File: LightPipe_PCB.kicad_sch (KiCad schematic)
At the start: 10 parts, among them X1 KLB-4, X2 KLB-4, X3 XT30, X4.1 Cable-0.7mm, X4.2 Cable-0.7mm, X5.1 Cable-1.5mm, X5.2 Cable-1.5mm

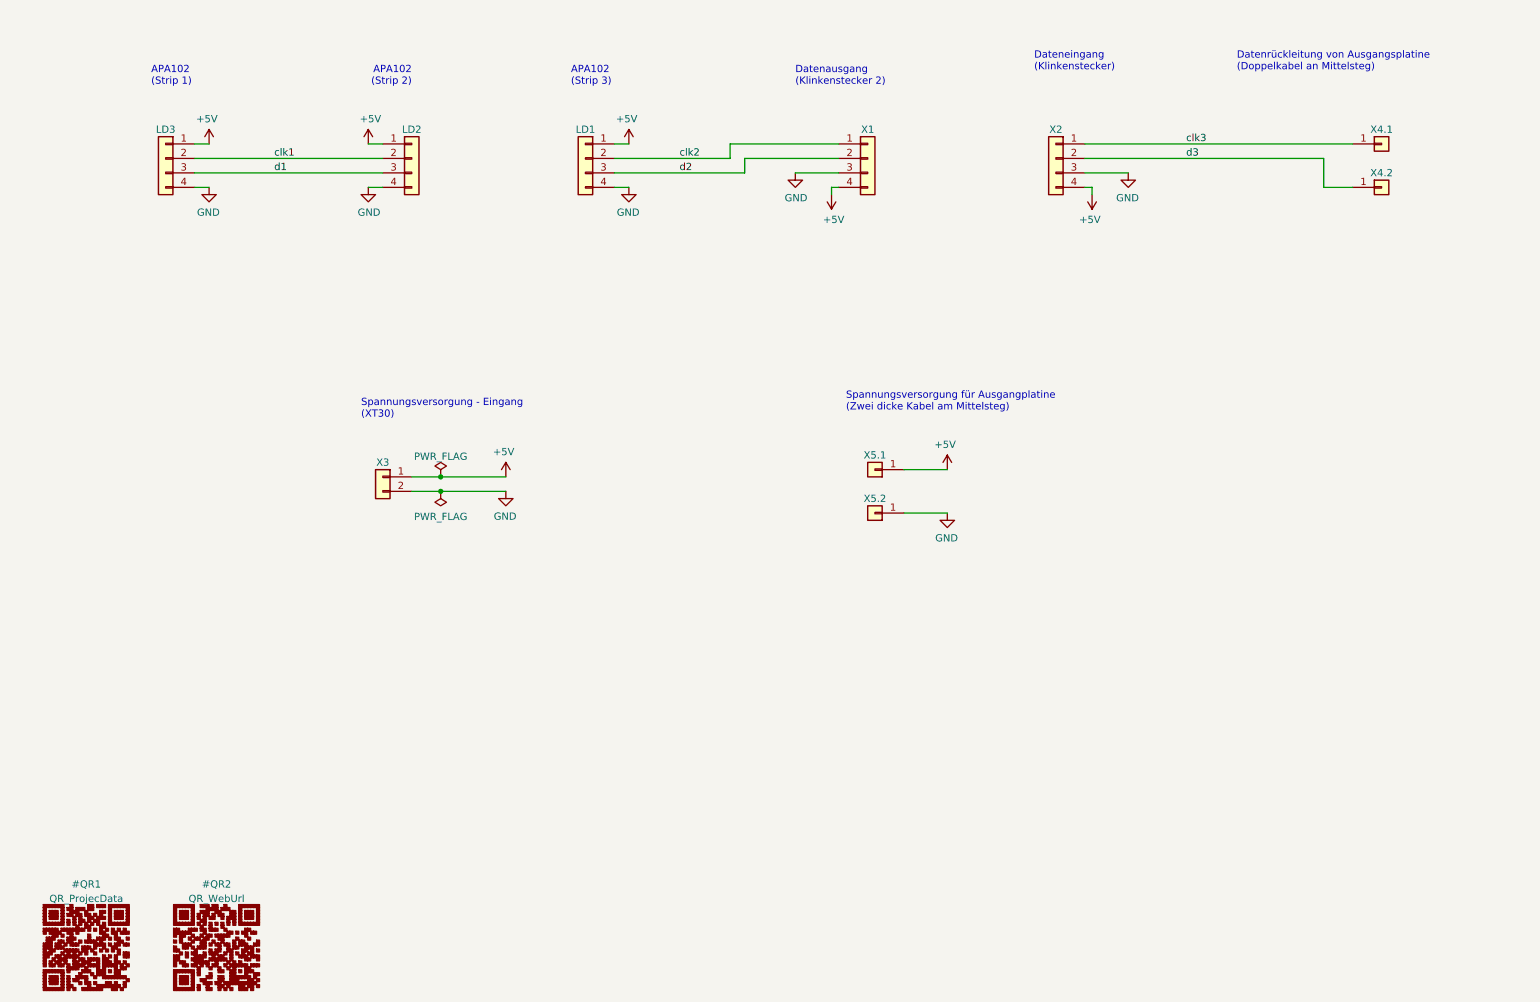
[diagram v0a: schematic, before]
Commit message: [clean] Optimized schematic to be easy readable as input PCB | changed 3D bodys in PCB to Input PCB positions | update date, company, project name and QR-code in schematic and board
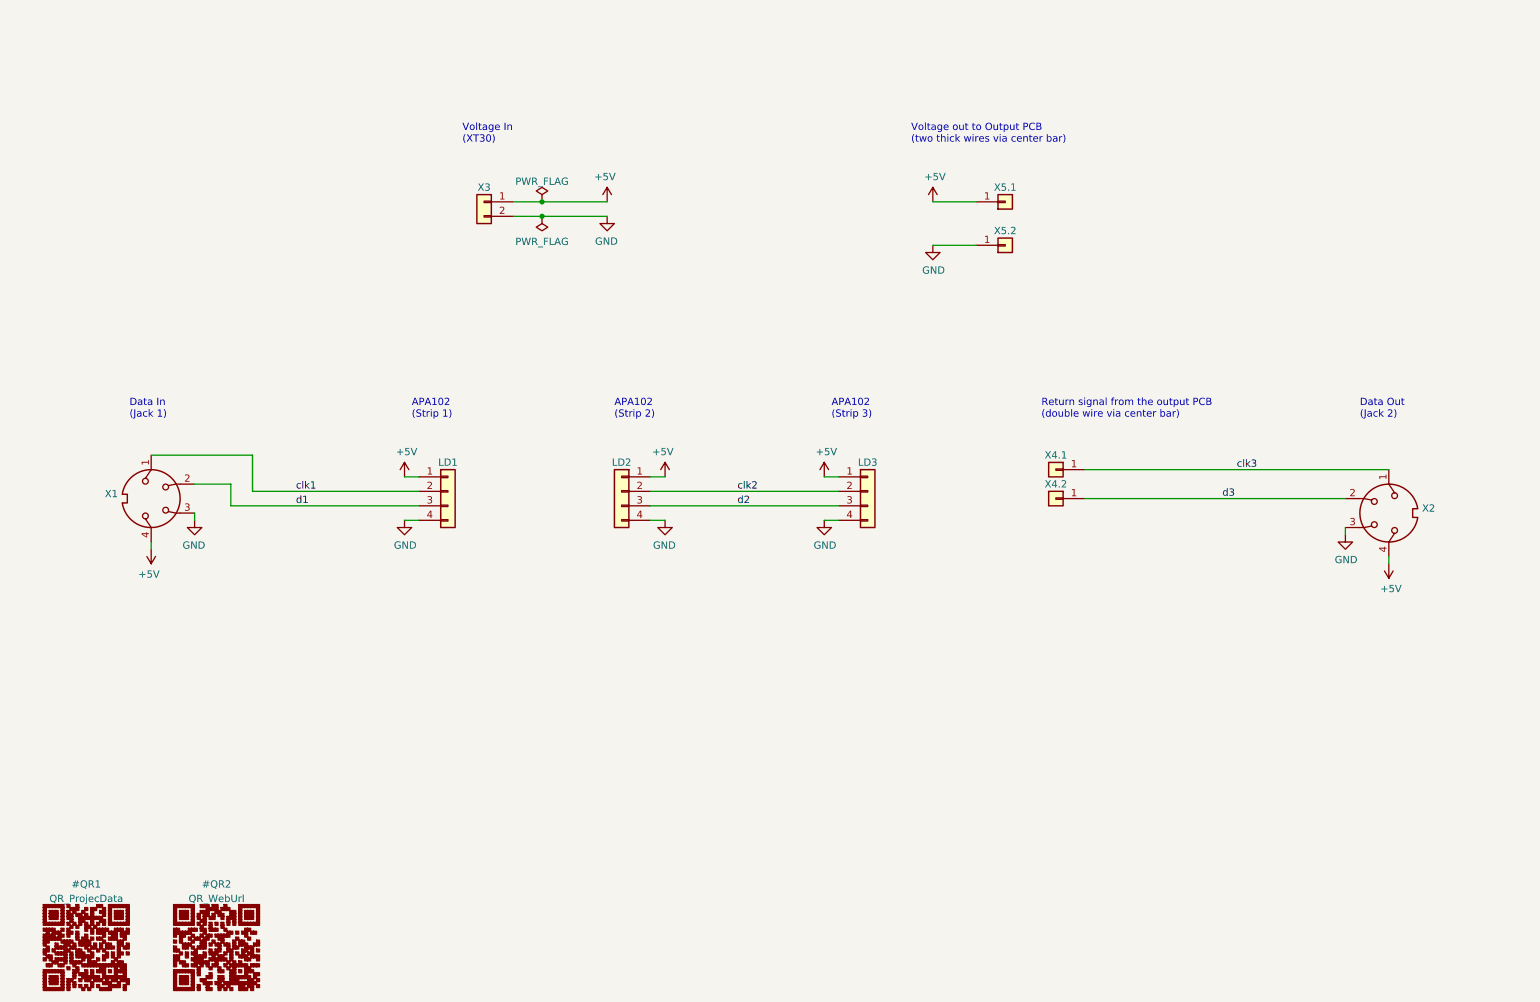
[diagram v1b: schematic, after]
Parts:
- removed X1, X2: KLB-4, h8-Connectors:Lumberg-KLB-4-Klinkensteckverbinder-3_5-180deg-turnable, symbol Connector_Generic:Conn_01x04
- added X1, X2: KLB-4, h8-Connectors:Lumberg-KLB-4-Klinkensteckverbinder-3_5-180deg-turnable, symbol Connector:DIN-4
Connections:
- net +5V: now also X1.4, X2.4
- net GND: now also X1.3, X2.3
- net clk1: now also LD1.2 (Pin_2), X1.1; no longer LD2.2 (Pin_2), LD3.2 (Pin_2)
- net clk2: now also LD2.2 (Pin_2), LD3.2 (Pin_2); no longer LD1.2 (Pin_2)
- net clk3: now also X2.1
- net d1: now also LD1.3 (Pin_3), X1.2; no longer LD2.3 (Pin_3), LD3.3 (Pin_3)
- net d2: now also LD2.3 (Pin_3), LD3.3 (Pin_3); no longer LD1.3 (Pin_3)
- net d3: now also X2.2
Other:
- note added: "Data In (Jack 1)"
- note added: "Data Out (Jack 2)"
- note added: "Return signal from the output PCB (double wire via center bar)"
- note added: "Voltage In (XT30)"
- note added: "Voltage out to Output PCB (two thick wires via center bar)"
- note removed: "Datenausgang (Klinkenstecker 2)"
- note removed: "Dateneingang (Klinkenstecker)"
- note removed: "Datenrückleitung von Ausgangsplatine (Doppelkabel an Mittelsteg)"
- note removed: "Spannungsversorgung - Eingang (XT30)"
- note removed: "Spannungsversorgung für Ausgangplatine (Zwei dicke Kabel am Mittelsteg)"
- company: CCC Göttingen -> HansAchterbahn
- title: LightPipe - StripeConnector -> LightPipe Input/Output PCB
- moved on the sheet: LD1, LD2, LD3, X3, X4.1, X4.2, X5.1, X5.2

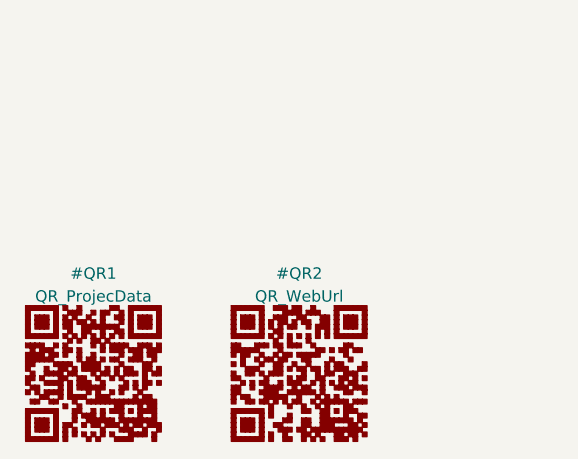
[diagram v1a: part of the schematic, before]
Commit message: [DRC] Solved DRC errors
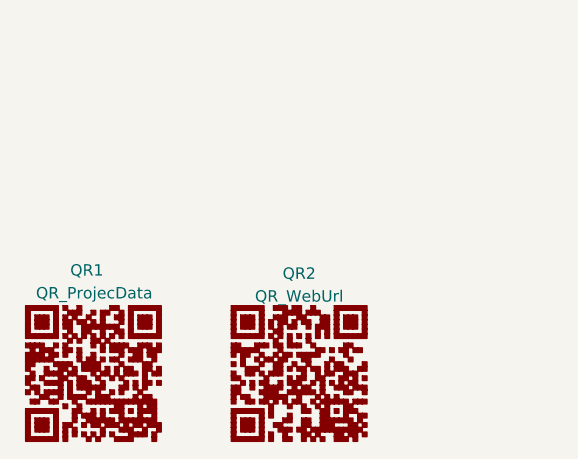
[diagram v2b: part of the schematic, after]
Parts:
- added QR1: QR_ProjecData, QR:QR_ProjecData, symbol QR_Lib:QR_ProjecData
- added QR2: QR_WebUrl, QR:QR_WebUrl, symbol QR_Lib:QR_WebUrl
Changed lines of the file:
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@@
   )
   (symbol (lib_id "QR_Lib:QR_ProjecData") (at 27.94 184.15 0) (unit 1)
-    (in_bom no) (on_board yes) (fields_autoplaced)
-    (property "Reference" "#QR1" (id 0) (at 27.98 173.0767 0))
-    (property "Value" "QR_ProjecData" (id 1) (at 27.98 175.6136 0))
+    (in_bom no) (on_board yes)
+    (property "Reference" "QR1" (id 0) (at 25.4 172.72 0)
+      (effects (font (size 1.27 1.27)) (justify left))
+    )
+    (property "Value" "QR_ProjecData" (id 1) (at 21.59 175.26 0)
+      (effects (font (size 1.27 1.27)) (justify left))
+    )
     (property "Footprint" "QR:QR_ProjecData" (id 2) (at 27.94 194.6 0)
       (effects (font (size 1.27 1.27)) hide)
@@
   (symbol (lib_id "QR_Lib:QR_WebUrl") (at 50.8 184.15 0) (unit 1)
     (in_bom no) (on_board yes) (fields_autoplaced)
-    (property "Reference" "#QR2" (id 0) (at 50.84 173.0767 0))
+    (property "Reference" "QR2" (id 0) (at 50.84 173.0767 0))
     (property "Value" "QR_WebUrl" (id 1) (at 50.84 175.6136 0))
     (property "Footprint" "QR:QR_WebUrl" (id 2) (at 50.8 194.6 0)
@@
       (reference "#PWR?") (unit 1) (value "+5V") (footprint "")
     )
-    (path "/8ca2c3de-1205-4532-8a76-d9c1a6b1f484"
-      (reference "#QR1") (unit 1) (value "QR_ProjecData") (footprint "QR:QR_ProjecData")
-    )
-    (path "/cb914536-84d3-4fd6-ba86-3661b57a5b27"
-      (reference "#QR2") (unit 1) (value "QR_WebUrl") (footprint "QR:QR_WebUrl")
-    )
     (path "/00000000-0000-0000-0000-00005f94ae24"
       (reference "LD1") (unit 1) (value "APA102") (footprint "h8-Connectors:APA102-Strip-Output")
@@
       (reference "LD3") (unit 1) (value "APA102") (footprint "h8-Connectors:APA102-Strip-Output")
     )
+    (path "/8ca2c3de-1205-4532-8a76-d9c1a6b1f484"
+      (reference "QR1") (unit 1) (value "QR_ProjecData") (footprint "QR:QR_ProjecData")
+    )
+    (path "/cb914536-84d3-4fd6-ba86-3661b57a5b27"
+      (reference "QR2") (unit 1) (value "QR_WebUrl") (footprint "QR:QR_WebUrl")
+    )
     (path "/c2774b4d-69cb-4b83-93d8-9a28fe6279cf"

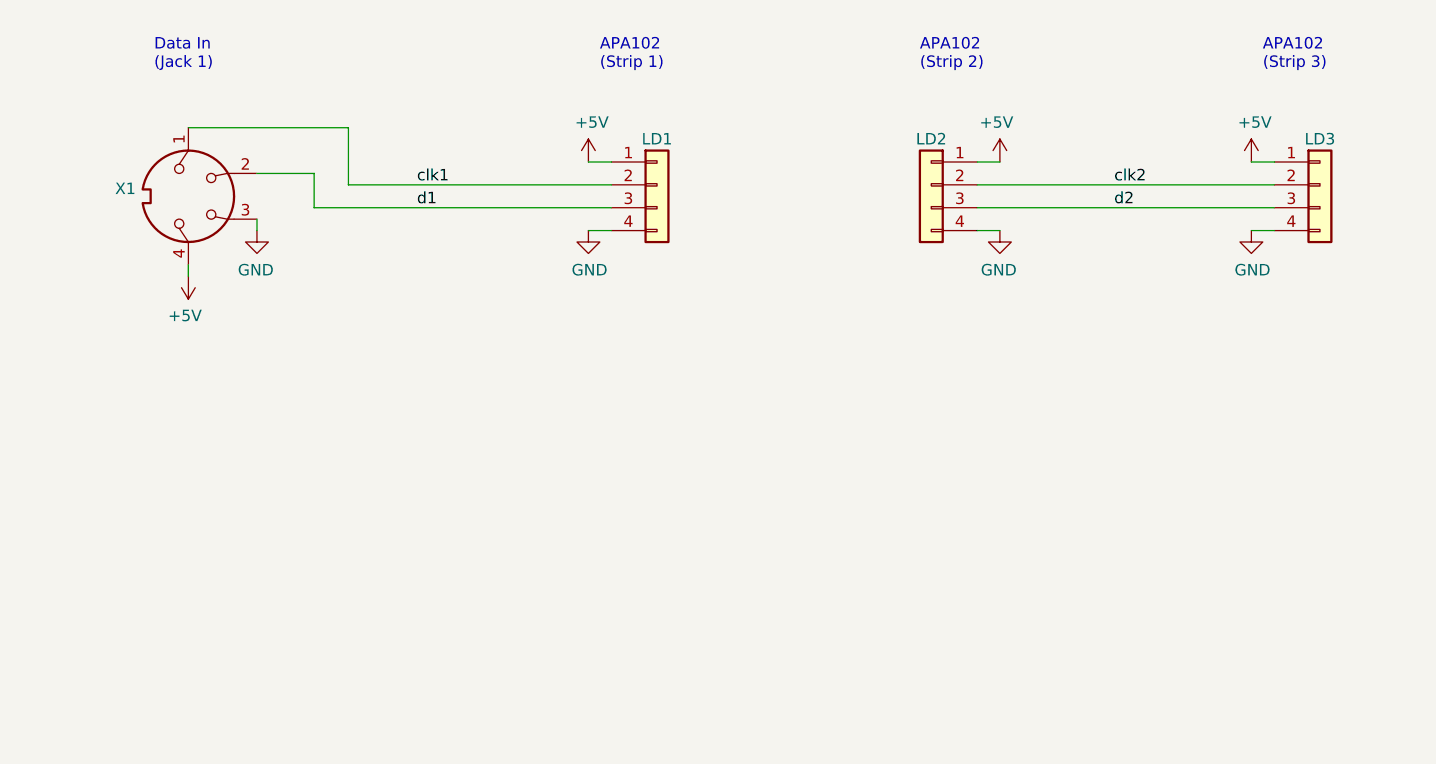
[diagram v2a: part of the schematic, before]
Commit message: [clean] improved schematic and pcb to be easier to read in Input-Mode
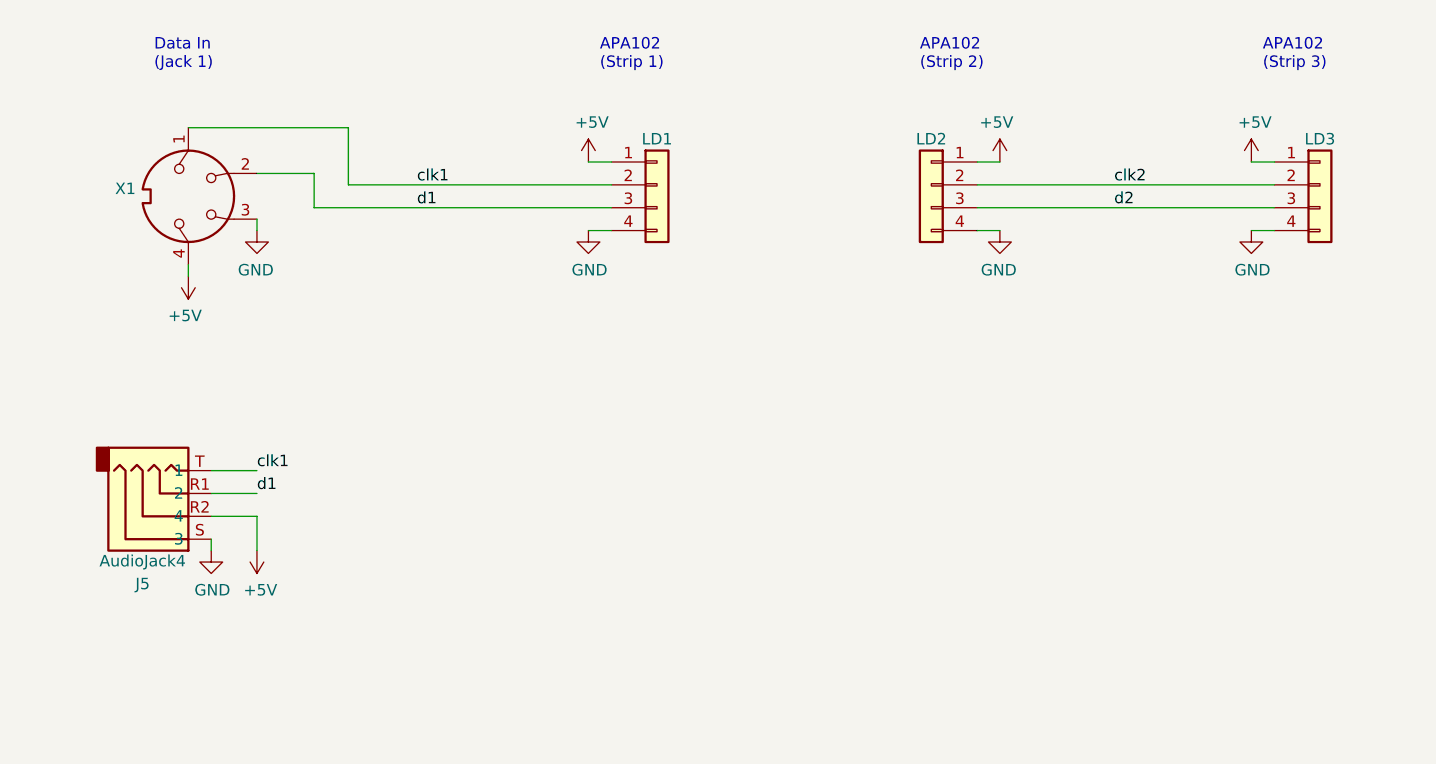
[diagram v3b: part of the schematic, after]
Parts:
- added J5: AudioJack4, h8-Connectors:Lumberg-KLB-4-Klinkensteckverbinder-3_5-180deg-turnable, symbol Connector:AudioJack4
- renumbered X4.2 to X4.1, X4.1 to X4.2
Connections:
- net +5V: now also J5.R2
- net GND: now also J5.S
- net clk1: now also J5.T
- net clk3: now also X4.1.1 (Pin_1); no longer X4.2.1 (Pin_1)
- net d1: now also J5.R1
- net d3: now also X4.2.1 (Pin_1); no longer X4.1.1 (Pin_1)
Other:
- moved on the sheet: X4.1, X4.2
